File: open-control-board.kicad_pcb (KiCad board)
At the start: 6 copper layers, 69 x 54 mm, 188 parts, among them CN1 LCC Port, CN14 Conn_02x06_Odd_Even, CN2 Conn_01x06_Pin, CN3 12V Separate Supply, CN4 Conn_02x05_Counter_Clockwise, CN5 NTC Brew Boiler, CN6 NTC Service Boiler, CN7 Conn_01x06_Pin, CN8 Conn_01x05_Pin, CN9 Conn_02x04, J1 USB_B_Micro, J13 Conn_02x05_Odd_Even, J15 Conn_02x05_Odd_Even, J16 USB_B_Micro, J17 BM04B-SRSS-TB(LF)(SN), J2 BM04B-SRSS-TB(LF)(SN), J3 Conn_02x03_Odd_Even, J4 Molex_0525591853, J5 Micro_SD_Card_Det_Hirose_DM3AT, Q1 DMP21D0UT-7, Q10 DMG1012T-7, Q11 DMN63D8LDW, Q12 DMN63D8LDW, Q13 DMG1012T-7, Q14 DMG1012T-7, Q15 DMP21D0UT-7, Q2 DMP21D0UT-7, Q3 Q_PMOS-E_DUAL_Generic_SEP_S1G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, Q4 DMN63D8LDW, Q5 Q_PMOS-E_DUAL_Generic_SEP_S1G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, Q6 DMN63D8LDW, Q7 DMN63D8LDW, Q8 DMP21D0UT-7, Q9 DMG1012T-7, SW1 SW_Push, SW2 SW_Push, SW3 SW_Push, SW4 SW_Push, U1 TPS82130, U10 FDC1004, U11 TC2014-5.0VxCTTR, U15 STPIC6C595TTR, U16 STPIC6C595TTR, U2 W25Q16JVUXIQ, U3 TPS82130, U4 RP2040, U5 ESP32-S3-WROOM-1, U6 ADS124S08IPBSR, U7 LM5050-1, U8 LM5050-1, U9 W25Q16JVUXIQ, Y1 XYDBPCNANF-12MHZ

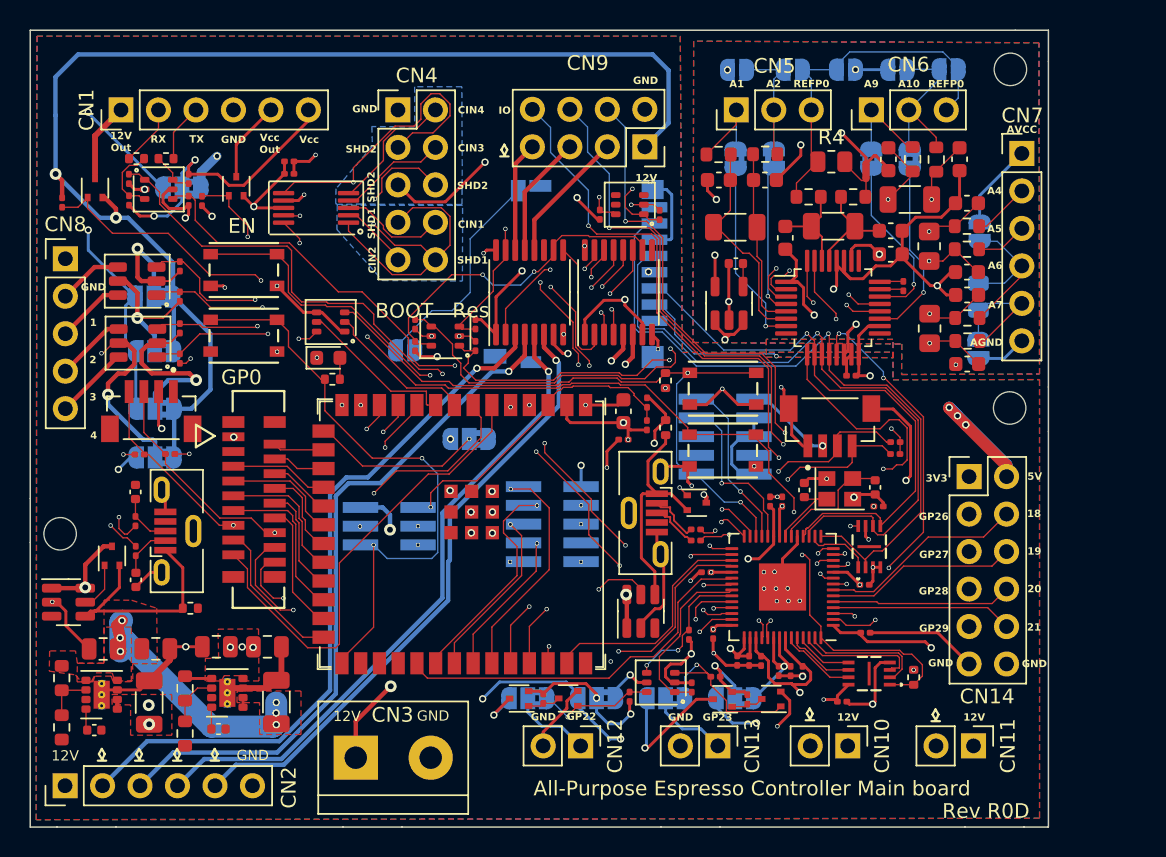
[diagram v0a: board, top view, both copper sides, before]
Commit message: Re-added LED and fixed silk screen
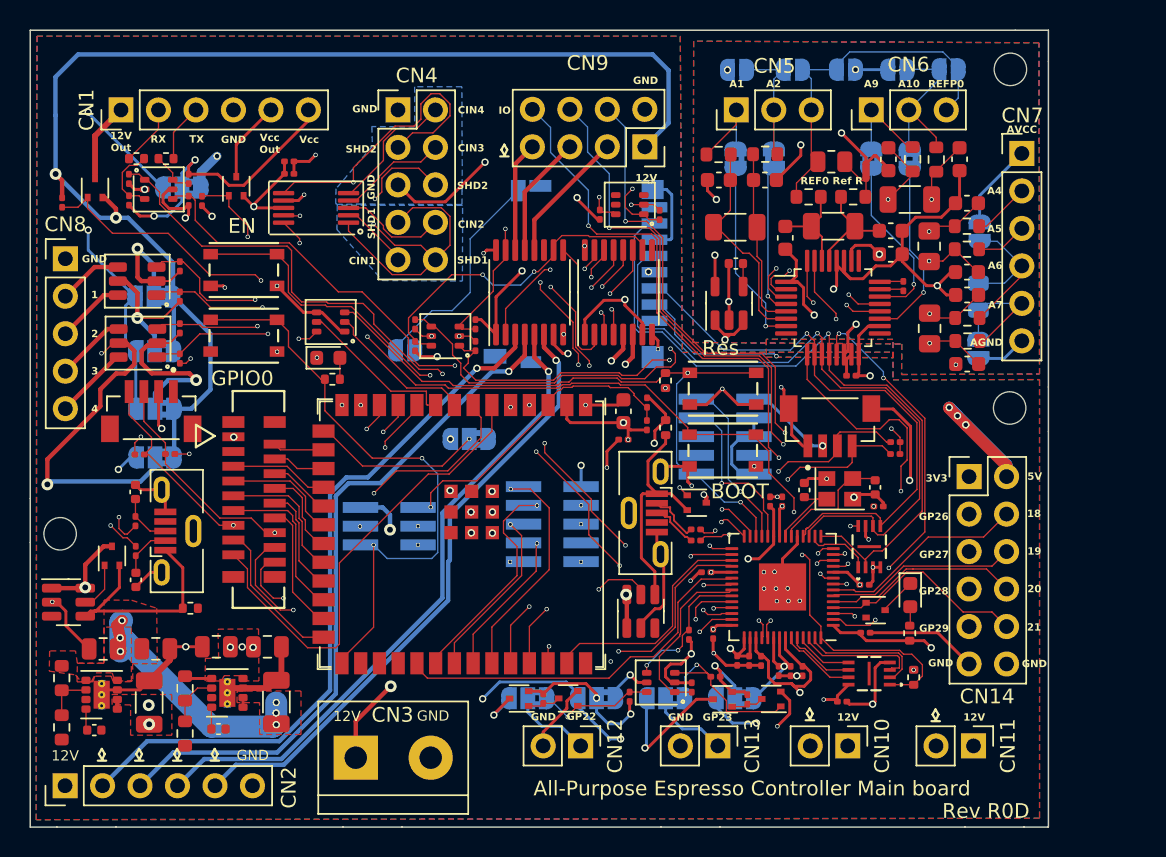
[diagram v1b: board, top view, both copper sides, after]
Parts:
- added D1: KT-0603W, LED_SMD:LED_0603_1608Metric, F.Cu at (111.6, 62.8)
- added Q16: DMG1012T-7, Package_TO_SOT_SMD:SOT-523, F.Cu at (109.3, 63.8)
- added R44: 120R, Resistor_SMD:R_0402_1005Metric, F.Cu at (111.6, 65.4)
- C39, C42: footprint Resistor_SMD:R_0805_2012Metric_Pad1.20x1.40mm_HandSolder -> Capacitor_SMD:C_0805_2012Metric_Pad1.18x1.45mm_HandSolder
- C48: value C_Small -> 6.8 nF, 50V
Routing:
- net Net-(JP16-C): track 19.8 -> 30.1 mm
- net Net-(D1-K): track 0.00 -> 2.51 mm
- net GND: track 186.2 -> 188.5 mm
- net CN14_10: track 12.3 -> 14.3 mm
- net Net-(D1-A): track 0.00 -> 1.30 mm
- net ADC_CS: track 28.7 -> 27.4 mm
- net +3V3: track 295.4 -> 294.3 mm
- net CN14_8: track 12.2 -> 13.2 mm
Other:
- board text added: "AIN10 - 5VA"
- board text added: "AIN10- REFP0"
- board text added: "AIN2 - 5VA"
- board text added: "AIN6/ REFP1 - 5VA"
- board text added: "AIN7/ REFN1 - GND"
- board text added: "CN12"
- board text added: "CN13"
- board text added: "GPIO0"
- board text added: "Hi-I Out"
- board text added: "JTAG"
- board text added: "Lo-I IO"
- board text added: "REF0 Ref R"
- board text added: "REF1 Ref R"
- board text added: "REFP0 - 5VA"
- board text added: "RES"
- board text added: "UART"
- board text removed: "A0"
- board text removed: "A3"
- board text removed: "ADC DRDY - GPIO18"
- board text removed: "AIN10 - REFP0"
- board text removed: "ESP-Prog JTAG"
- board text removed: "ESP-Prog UART"
- board text removed: "GP18"
- board text removed: "GP19"
- board text removed: "GP20"
- board text removed: "GP21"
- board text removed: "LED - CN12"
- board text removed: "RESET"

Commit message: Updated docs
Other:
- board text removed: "CN10 UART TX Verified"
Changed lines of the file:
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@@
     (attr exclude_from_pos_files exclude_from_bom)
     (net_tie_pad_groups "1, 2, 3")
-    (fp_text reference "JP5" (at 12.43 3.15) (layer "B.SilkS") hide
+    (fp_text reference "JP5" (at -0.03 -0.11) (layer "B.SilkS") hide
         (effects (font (size 1 1) (thickness 0.15)) (justify mirror))
     )
@@
     (effects (font (size 0.5 0.5) (thickness 0.1) bold) (justify bottom))
   )
-  (gr_text "CN10 UART TX Verified" (at 55.75 20.825) (layer "Cmts.User")
-    (effects (font (size 1 1) (thickness 0.15)) (justify left bottom))
-  )
   (segment (start 55.7775 70.505) (end 55.7775 71.8475) (width 0.09) (layer "F.Cu") (net 1))

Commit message: Updated capacitor footprint
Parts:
- C39, C42: footprint Capacitor_SMD:C_0805_2012Metric_Pad1.18x1.45mm_HandSolder -> Capacitor_SMD:C_1206_3216Metric_Pad1.33x1.80mm_HandSolder
- moved C39 0.77 mm to (112.6, 45.4)
- moved C42 0.73 mm to (112.6, 39.8)
- moved C35 0.52 mm to (109.8, 38.1)
- moved C46 0.52 mm to (109.8, 39.7)
- moved C28 0.51 mm to (105.9, 37.8)
- moved C3 0.48 mm to (99.3, 37.8)
- moved C29 0.47 mm to (102.7, 38.6)
- moved C47 0.47 mm to (110.7, 41.8)
- moved U6 0.40 mm to (106.0, 43.3)
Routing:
- net GND: track 188.5 -> 182.4 mm, vias 60 -> 62
- net +3V3: track 294.3 -> 296.5 mm
- net AIN5: track 17.4 -> 19.2 mm
- net AIN7_REFN1: track 15.8 -> 17.1 mm
- net AIN8: track 11.9 -> 11.2 mm
- net REFN0: track 7.30 -> 6.66 mm

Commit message: Added more power connectors to CN9
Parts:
- added CN9_PWR1: Conn_01x04_Pin, Connector_PinHeader_2.54mm:PinHeader_1x04_P2.54mm_Vertical, F.Cu at (86.0, 27.3)
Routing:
- net +5V: track 278.7 -> 312.8 mm, vias 21 -> 32
- net +3V3: track 296.5 -> 308.0 mm
- net GND: track 182.4 -> 182.1 mm, vias 62 -> 65
